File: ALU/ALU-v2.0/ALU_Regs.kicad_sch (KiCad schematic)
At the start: 9 parts, among them U12 74ACT04, U13 74ACT00, U14 74ACT32, U19 74ACT08, U22 74ACT02, U66 74LVC1G125

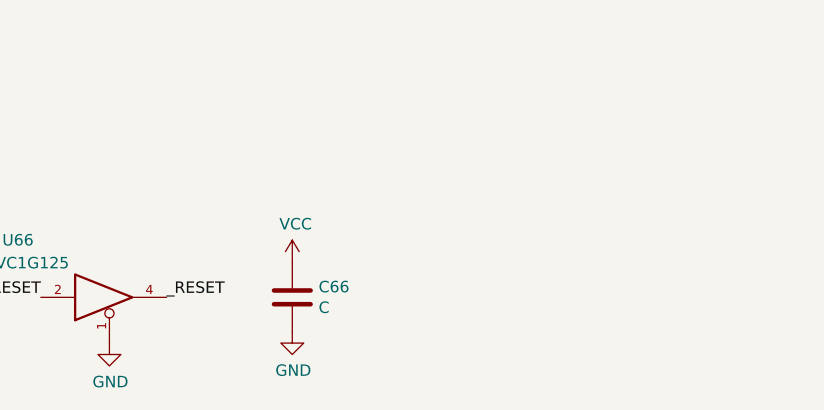
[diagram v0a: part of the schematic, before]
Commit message: button up all missing things, generate groundplanes on all signal layers
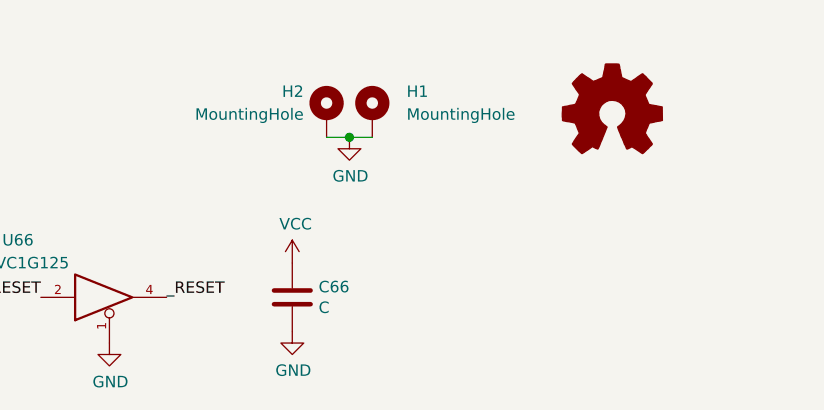
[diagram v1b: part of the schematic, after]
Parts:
- added H1, H2: MountingHole, Schroff:Hole 2.8mm, symbol Mechanical:MountingHole_Pad
- added LOGO1: Logo_Open_Hardware_Small, Symbol:OSHW-Logo2_9.8x8mm_SilkScreen, symbol Graphic:Logo_Open_Hardware_Small
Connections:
- net GND: now also H1.1, H2.1
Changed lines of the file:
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@@
   (junction (at 57.15 349.25) (diameter 1.016) (color 0 0 0 0))
   (junction (at 57.15 354.33) (diameter 1.016) (color 0 0 0 0))
+  (junction (at 124.46 27.94) (diameter 1.016) (color 0 0 0 0))
   (junction (at 251.46 29.21) (diameter 1.016) (color 0 0 0 0))
   (junction (at 251.46 67.31) (diameter 1.016) (color 0 0 0 0))
@@
   (junction (at 254 196.85) (diameter 1.016) (color 0 0 0 0))
   (junction (at 254 257.81) (diameter 1.016) (color 0 0 0 0))
-  (no_connect (at 72.39 280.67))
-  (no_connect (at 72.39 337.82))
-  (no_connect (at 72.39 223.52))
-  (no_connect (at 72.39 295.91))
-  (no_connect (at 72.39 266.7))
   (no_connect (at 72.39 251.46))
-  (no_connect (at 72.39 237.49))
   (no_connect (at 72.39 323.85))
+  (no_connect (at 72.39 223.52))
+  (no_connect (at 72.39 237.49))
   (no_connect (at 72.39 309.88))
+  (no_connect (at 72.39 295.91))
+  (no_connect (at 72.39 337.82))
   (no_connect (at 72.39 351.79))
+  (no_connect (at 72.39 266.7))
+  (no_connect (at 72.39 280.67))
   (bus_entry (at 85.09 146.05) (size 2.54 -2.54)
     (stroke (width 0.1524) (type solid) (color 0 0 0 0))
@@
     (stroke (width 0) (type solid) (color 0 0 0 0))
   )
+  (wire (pts (xy 121.92 27.94) (xy 124.46 27.94))
+    (stroke (width 0) (type solid) (color 0 0 0 0))
+  )
+  (wire (pts (xy 124.46 27.94) (xy 127 27.94))
+    (stroke (width 0) (type solid) (color 0 0 0 0))
+  )
   (wire (pts (xy 132.08 115.57) (xy 148.59 115.57))
     (stroke (width 0) (type solid) (color 0 0 0 0))
@@
   (symbol (lib_id "power:VCC") (at 45.72 20.32 0) (unit 1)
     (in_bom yes) (on_board yes)
-    (property "Reference" "#PWR?" (id 0) (at 45.72 24.13 0)
+    (property "Reference" "#PWR0115" (id 0) (at 45.72 24.13 0)
       (effects (font (size 1.27 1.27)) hide)
     )
@@
   (symbol (lib_id "power:GND") (at 43.18 271.78 0) (unit 1)
     (in_bom yes) (on_board yes)
-    (property "Reference" "#PWR?" (id 0) (at 43.18 278.13 0)
+    (property "Reference" "#PWR0110" (id 0) (at 43.18 278.13 0)
       (effects (font (size 1.27 1.27)) hide)
     )
@@
     )
   )
+  (symbol (lib_id "power:GND") (at 124.46 27.94 0) (unit 1)
+    (in_bom yes) (on_board yes)
+    (property "Reference" "#PWR0116" (id 0) (at 124.46 34.29 0)
+      (effects (font (size 1.27 1.27)) hide)
+    )
+    (property "Value" "GND" (id 1) (at 124.5743 32.2644 0))
+    (property "Footprint" "" (id 2) (at 124.46 27.94 0)
+      (effects (font (size 1.27 1.27)) hide)
+    )
+    (property "Datasheet" "" (id 3) (at 124.46 27.94 0)
+      (effects (font (size 1.27 1.27)) hide)
+    )
+  )
   (symbol (lib_id "power:GND") (at 254 257.81 0) (unit 1)
     (in_bom yes) (on_board yes)
@@
     )
   )
+  (symbol (lib_id "Mechanical:MountingHole_Pad") (at 121.92 25.4 0) (unit 1)
+    (in_bom yes) (on_board yes)
+    (property "Reference" "H2" (id 0) (at 119.38 22.86 0)
+      (effects (font (size 1.27 1.27)) (justify right))
+    )
+    (property "Value" "MountingHole" (id 1) (at 119.38 25.4 0)
+      (effects (font (size 1.27 1.27)) (justify right))
+    )
+    (property "Footprint" "Schroff:Hole 2.8mm" (id 2) (at 121.92 25.4 0)
+      (effects (font (size 1.27 1.27)) hide)
+    )
+    (property "Datasheet" "~" (id 3) (at 121.92 25.4 0)
+      (effects (font (size 1.27 1.27)) hide)
+    )
+  )
+  (symbol (lib_id "Mechanical:MountingHole_Pad") (at 127 25.4 0) (unit 1)
+    (in_bom yes) (on_board yes)
+    (property "Reference" "H1" (id 0) (at 130.81 22.86 0)
+      (effects (font (size 1.27 1.27)) (justify left))
+    )
+    (property "Value" "MountingHole" (id 1) (at 130.81 25.4 0)
+      (effects (font (size 1.27 1.27)) (justify left))
+    )
+    (property "Footprint" "Schroff:Hole 2.8mm" (id 2) (at 127 25.4 0)
+      (effects (font (size 1.27 1.27)) hide)
+    )
+    (property "Datasheet" "~" (id 3) (at 127 25.4 0)
+      (effects (font (size 1.27 1.27)) hide)
+    )
+  )
   (symbol (lib_id "Device:C") (at 118.11 45.72 0) (unit 1)
     (in_bom yes) (on_board yes)
@@
     )
   )
+  (symbol (lib_id "Graphic:Logo_Open_Hardware_Small") (at 153.67 25.4 0) (unit 1)
+    (in_bom yes) (on_board yes)
+    (property "Reference" "LOGO1" (id 0) (at 153.67 18.415 0)
+      (effects (font (size 1.27 1.27)) hide)
+    )
+    (property "Value" "Logo_Open_Hardware_Small" (id 1) (at 153.67 31.115 0)
+      (effects (font (size 1.27 1.27)) hide)
+    )
+    (property "Footprint" "Symbol:OSHW-Logo2_9.8x8mm_SilkScreen" (id 2) (at 153.67 25.4 0)
+      (effects (font (size 1.27 1.27)) hide)
+    )
+    (property "Datasheet" "~" (id 3) (at 153.67 25.4 0)
+      (effects (font (size 1.27 1.27)) hide)
+    )
+  )
   (symbol (lib_id "74xGxx:74LVC1G125") (at 97.79 45.72 0) (mirror x) (unit 1)
     (in_bom yes) (on_board yes)
@@
       (reference "#PWR0109") (unit 1)
     )
+    (path "/5187b3b4-bffb-442a-9fcb-bc0630441cd8"
+      (reference "#PWR0110") (unit 1)
+    )
+    (path "/1ee63a50-b801-45d4-997e-199f4b35aa7e"
+      (reference "#PWR0115") (unit 1)
+    )
+    (path "/c6d089b8-af23-4593-a43d-5ef54be714e1"
+      (reference "#PWR0116") (unit 1)
+    )
     (path "/00000000-0000-0000-0000-00006098ca23"
       (reference "#PWR0261") (unit 1)
@@
       (reference "#PWR0263") (unit 1)
     )
-    (path "/1ee63a50-b801-45d4-997e-199f4b35aa7e"
-      (reference "#PWR?") (unit 1)
-    )
-    (path "/5187b3b4-bffb-442a-9fcb-bc0630441cd8"
-      (reference "#PWR?") (unit 1)
-    )
     (path "/dcce0d53-42a2-4fc5-acb2-9d5d91481967"
       (reference "C66") (unit 1)
     )
+    (path "/3fd2ca9a-e82c-431d-837e-b22289c449f9"
+      (reference "H1") (unit 1)
+    )
+    (path "/dfde1514-8c07-4e5e-b801-0f5f15de499b"
+      (reference "H2") (unit 1)
+    )
     (path "/00000000-0000-0000-0000-00005f547ccc"
       (reference "J_LEFT1") (unit 1)
@@
       (reference "J_RIGHT1") (unit 1)
     )
+    (path "/de631874-9bde-44f9-8594-3dc9c7583ed3"
+      (reference "LOGO1") (unit 1)
+    )
     (path "/00000000-0000-0000-0000-00005f4fcba6"

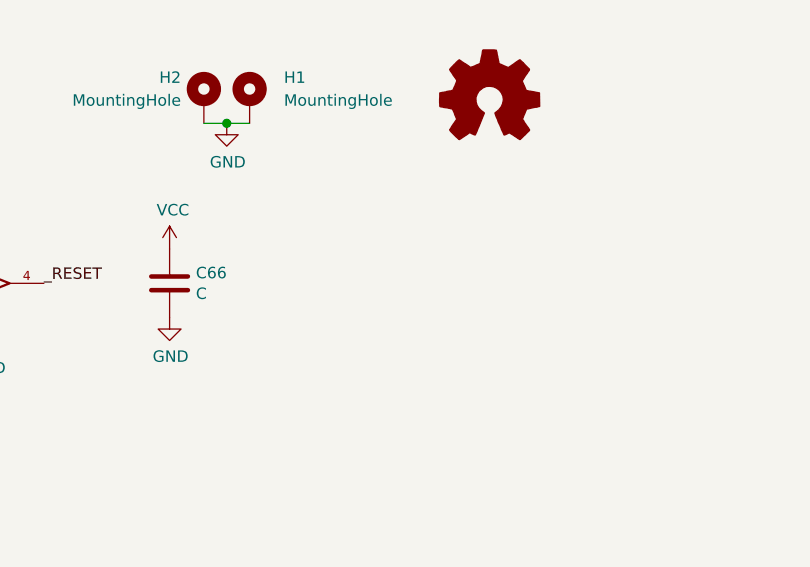
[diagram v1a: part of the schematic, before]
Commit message: added a power LED
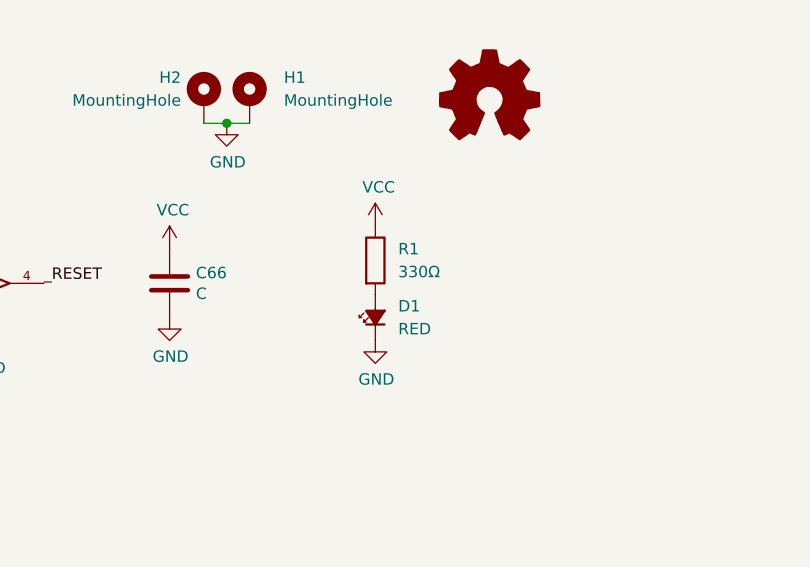
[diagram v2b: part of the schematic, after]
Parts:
- added D1: RED, LED_SMD:LED_0805_2012Metric, symbol Device:LED_Small_ALT
- added R1: 330Ω, Resistor_SMD:R_0805_2012Metric, symbol Device:R
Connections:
- net GND: now also D1.1 (K)
- net VCC: now also R1.1
- new net: D1.2 (A), R1.2

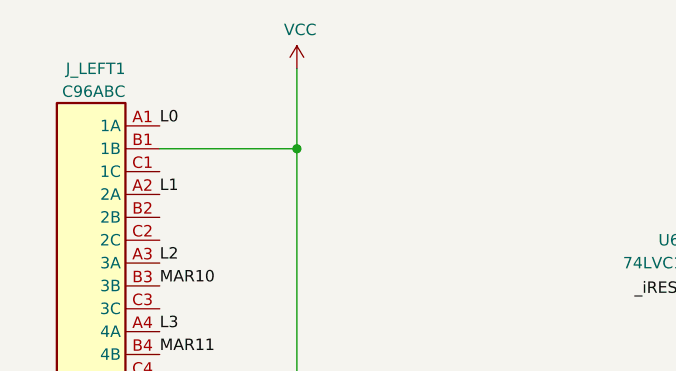
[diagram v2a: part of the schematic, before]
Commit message: change all caps to 0805
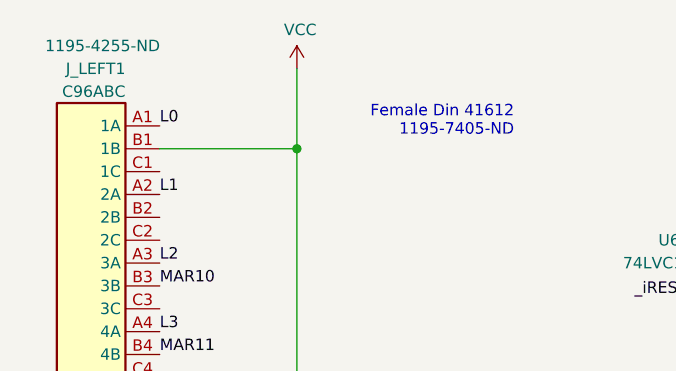
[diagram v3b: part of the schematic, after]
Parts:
- C66: footprint Capacitor_SMD:C_1206_3216Metric -> Capacitor_SMD:C_0805_2012Metric
- J_LEFT1: Digikey (none) -> 1195-4255-ND‎
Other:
- note added: "Female Din 41612 1195-7405-ND‎"
